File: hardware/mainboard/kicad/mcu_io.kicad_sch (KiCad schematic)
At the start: 30 parts, among them J2 Hirose DM3AT-SF-PEJM5, SW2 BOOT / RECOVERY, SW3 BTN_L1, SW4 BTN_L2, SW5 BTN_R1, SW6 BTN_R2, U1 ESP32-S3-WROOM-1-N16R8, U5 BMI270, U9 TMUX1101DBVR

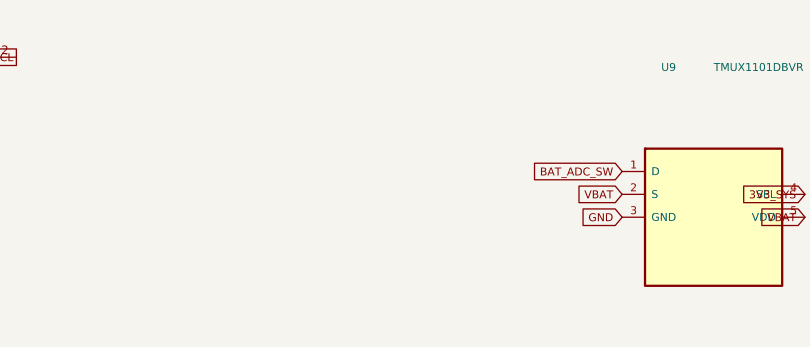
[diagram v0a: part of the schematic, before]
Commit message: R34: physically justified ERC power source flags on switched SYS_EN and pack GND
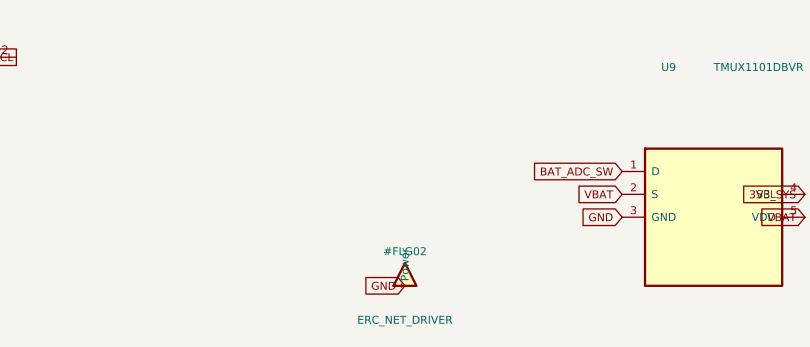
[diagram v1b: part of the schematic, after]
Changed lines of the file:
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@@
 	(global_label "3V3_SYS" (shape input) (at 359.41 182.88 0) (effects (font (size 0.88 0.88)) (justify right bottom)))
 	(global_label "GND" (shape input) (at 374.65 182.88 180) (effects (font (size 0.88 0.88)) (justify right bottom)))
+	(symbol (lib_id "ENKU:ERC_NET_DRIVER") (at 295.91 182.88 0) (unit 1) (exclude_from_sim no) (in_bom no) (on_board no) (dnp no)
+  (property "Reference" "#FLG02" (at 295.91 179.07 0) (effects (font (size 0.88 0.88))))
+  (property "Value" "ERC_NET_DRIVER" (at 295.91 186.69 0) (effects (font (size 0.88 0.88))))
+  (property "Footprint" "" (at 295.91 182.88 0) (effects (font (size 0.88 0.88)) (hide yes)))
+  (property "Datasheet" "~" (at 295.91 182.88 0) (effects (font (size 0.88 0.88)) (hide yes)))
+  (pin "1")
+  (instances (project "enku-mainboard-r0.1" (path "/10000000-0000-4000-8000-000000000001/e4200000-0000-4000-8000-000000000020" (reference "#FLG02") (unit 1))))
 )
+(global_label "GND" (shape input) (at 295.91 182.88 0) (effects (font (size 0.88 0.88)) (justify right bottom)))
+)

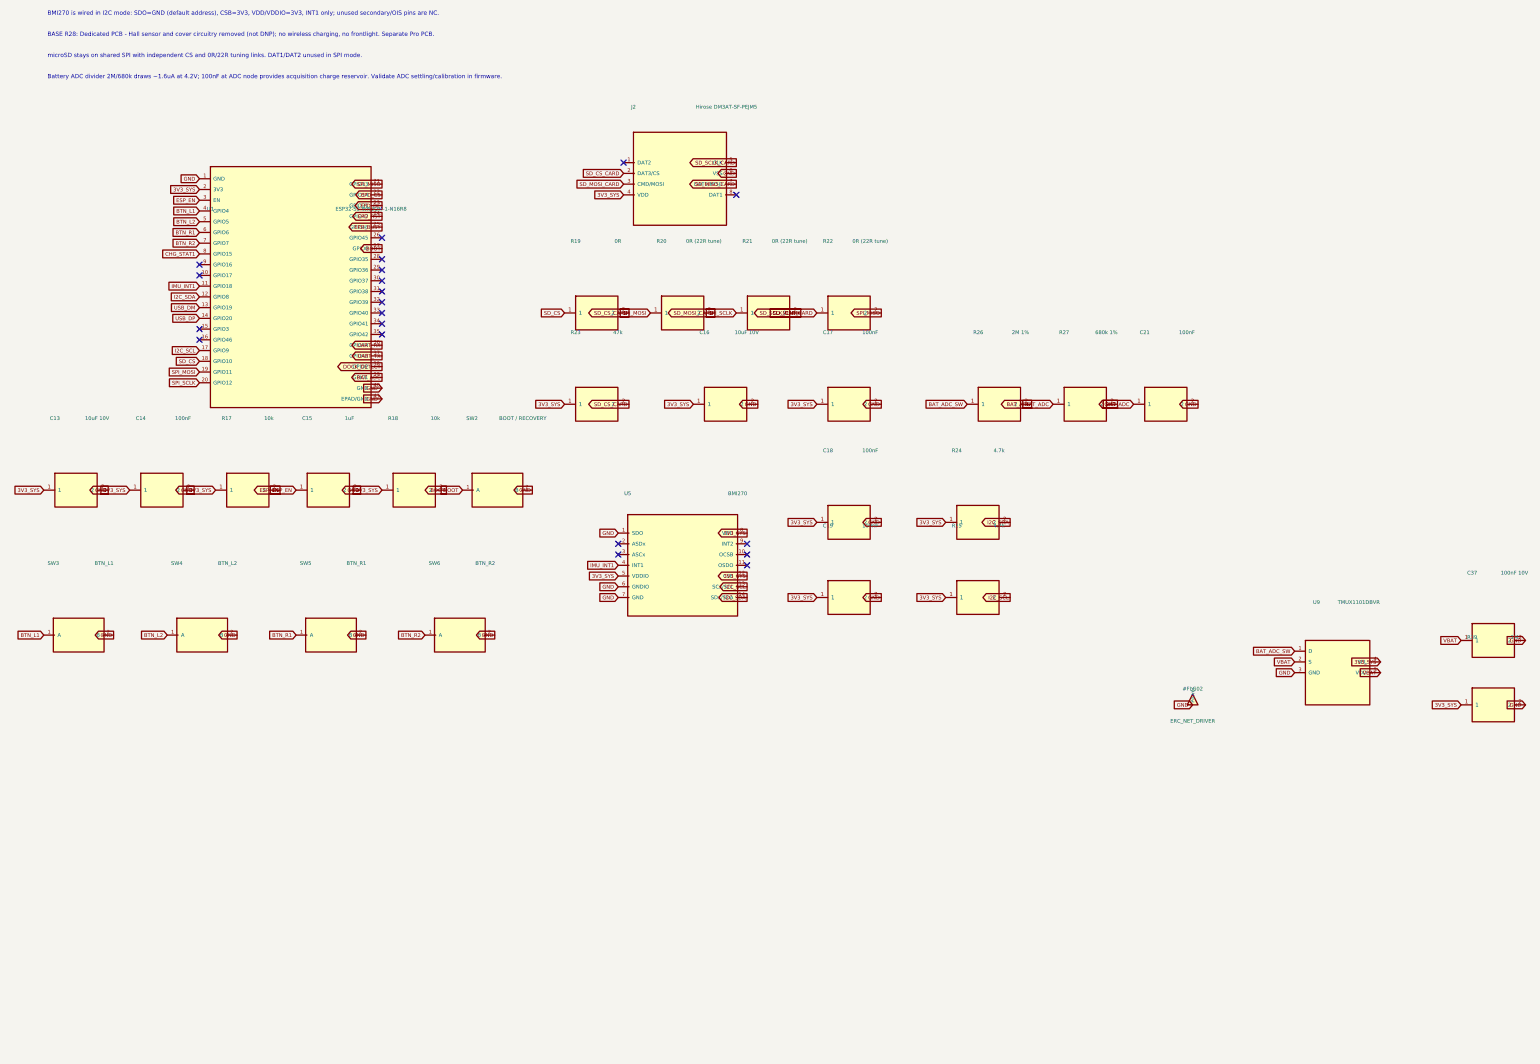
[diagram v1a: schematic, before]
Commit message: R41: implement switched-rail fail-safe VBUS comparator, discharge model, SD supply and dual ground references
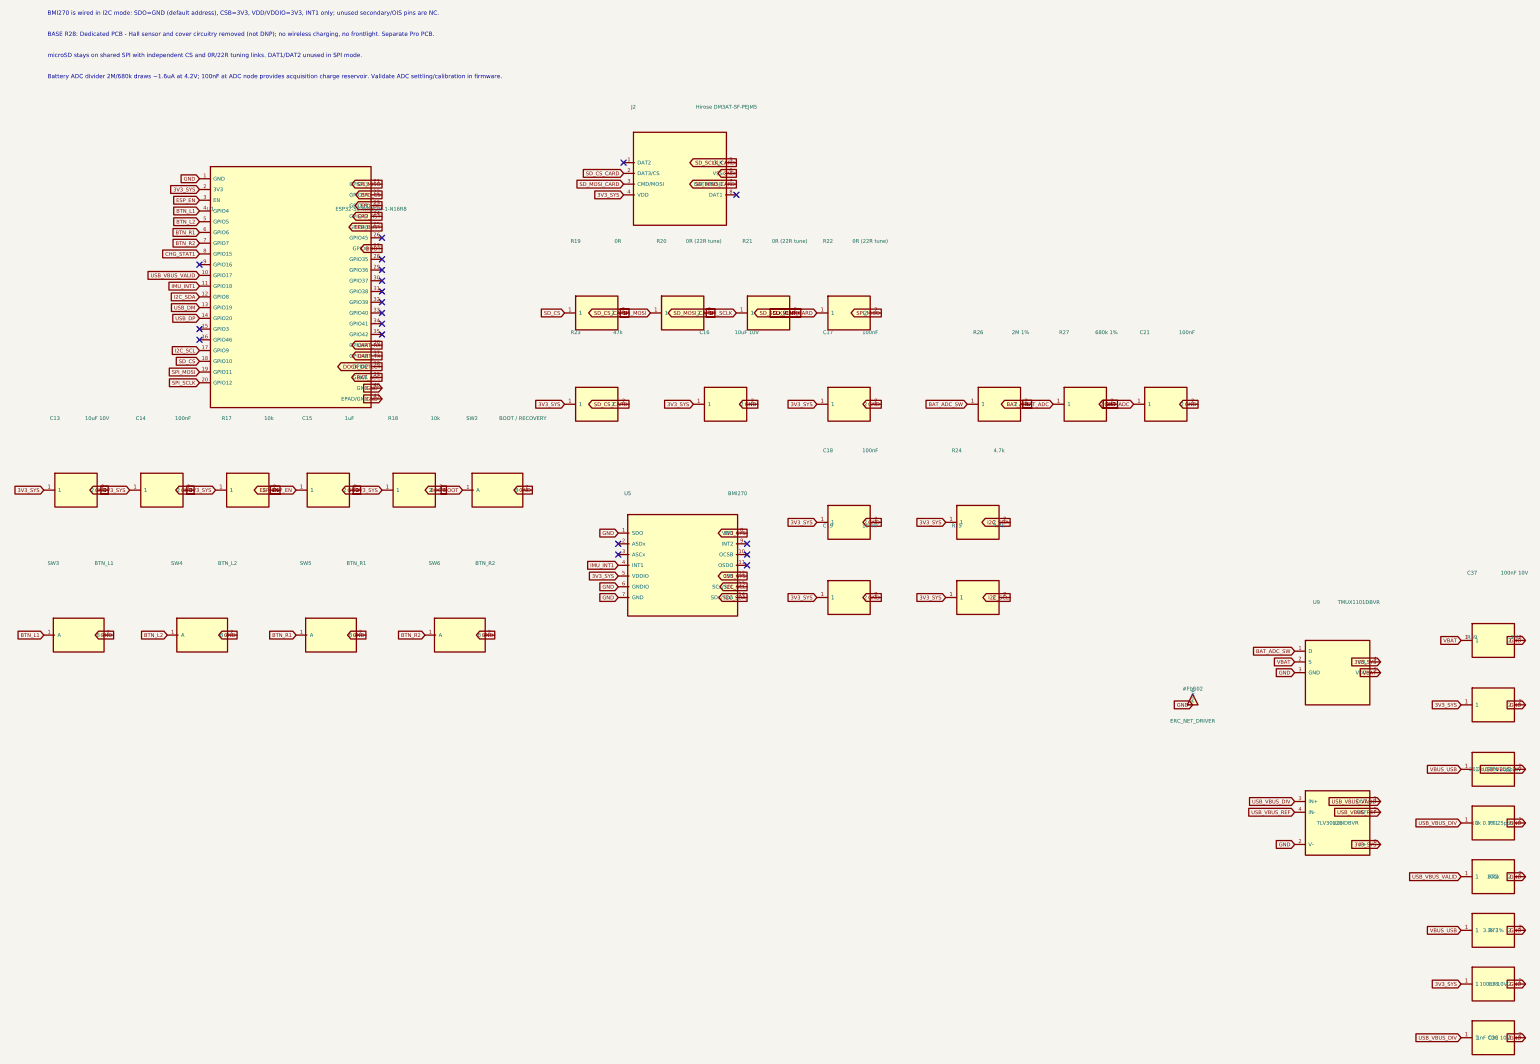
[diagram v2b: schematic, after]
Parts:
- added C38: 100nF 10V, Capacitor_SMD:C_0603_1608Metric, symbol ENKU:C
- added C39: 1nF C0G 10V, Capacitor_SMD:C_0603_1608Metric, symbol ENKU:C
- added R70: 26.7k 0.1% 25ppm, Resistor_SMD:R_0603_1608Metric, symbol ENKU:R
- added R71: 10k 0.1% 25ppm, Resistor_SMD:R_0603_1608Metric, symbol ENKU:R
- added R72: 100k, Resistor_SMD:R_0603_1608Metric, symbol ENKU:R
- added R73: 3.3k 1%, Resistor_SMD:R_0603_1608Metric, symbol ENKU:R
- added U10: TLV3012BIDBVR, ENKU:TLV3012B_DBV0006A, symbol ENKU:TLV3012B
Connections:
- net 3V3_SYS: now also C38.1, U10.6 (V+)
- net GND: now also C38.2, C39.2, R71.2, R72.2, R73.2, U10.2 (V-)
- net USB_VBUS_VALID: now reaches U1.10 (GPIO17)
- net USB_VBUS_VALID: now also R72.1, U10.1 (OUT)
- new net USB_VBUS_DIV: C39.1, R70.2, R71.1, U10.3 (IN+)
- new net USB_VBUS_REF: U10.4 (IN-), U10.5 (REF)
- new net VBUS_USB: R70.1, R73.1
- no-connect marks 20 -> 19
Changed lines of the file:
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@@
 	(global_label "CHG_STAT1" (shape input) (at 60.96 76.2 0) (effects (font (size 0.88 0.88)) (justify right bottom)))
 	(no_connect (at 60.96 78.74))
-	(no_connect (at 60.96 81.28))
+	(global_label "USB_VBUS_VALID" (shape input) (at 60.96 81.28 0) (effects (font (size 0.88 0.88)) (justify right bottom)))
 	(global_label "IMU_INT1" (shape input) (at 60.96 83.82 0) (effects (font (size 0.88 0.88)) (justify right bottom)))
 	(global_label "I2C_SDA" (shape input) (at 60.96 86.36 0) (effects (font (size 0.88 0.88)) (justify right bottom)))
@@
 )
 (global_label "GND" (shape input) (at 295.91 182.88 0) (effects (font (size 0.88 0.88)) (justify right bottom)))
+(symbol (lib_id "ENKU:TLV3012B") (at 330.2 210.82 0) (unit 1) (exclude_from_sim no) (in_bom yes) (on_board yes) (dnp no)
+(property "Reference" "U10" (at 330.2 210.82 0) (effects (font (size 0.88 0.88))))
+(property "Value" "TLV3012BIDBVR" (at 330.2 210.82 0) (effects (font (size 0.88 0.88))))
+(property "Footprint" "ENKU:TLV3012B_DBV0006A" (at 330.2 210.82 0) (effects (font (size 0.88 0.88)) (hide yes)))
+(property "Datasheet" "https://www.ti.com/lit/gpn/TLV3012B" (at 330.2 210.82 0) (effects (font (size 0.88 0.88)) (hide yes)))
+(property "Description" "TLV3012BIDBVR" (at 330.2 210.82 0) (effects (font (size 0.88 0.88)) (hide yes)))
+(pin "1")
+(pin "2")
+(pin "3")
+(pin "4")
+(pin "5")
+(pin "6")
+(instances (project "enku-mainboard-r0.1" (path "/10000000-0000-4000-8000-000000000001/769db365-4ac6-4285-9803-94ba4cec03fc" (reference "U10") (unit 1)))))
+(global_label "USB_VBUS_VALID" (shape input) (at 340.36 205.74 180) (effects (font (size 0.88 0.88)) (justify right bottom)))
+(global_label "GND" (shape input) (at 320.04 215.9 0) (effects (font (size 0.88 0.88)) (justify right bottom)))
+(global_label "USB_VBUS_DIV" (shape input) (at 320.04 205.74 0) (effects (font (size 0.88 0.88)) (justify right bottom)))
+(global_label "USB_VBUS_REF" (shape input) (at 320.04 208.28 0) (effects (font (size 0.88 0.88)) (justify right bottom)))
+(global_label "USB_VBUS_REF" (shape input) (at 340.36 208.28 180) (effects (font (size 0.88 0.88)) (justify right bottom)))
+(global_label "3V3_SYS" (shape input) (at 340.36 215.9 180) (effects (font (size 0.88 0.88)) (justify right bottom)))
+(symbol (lib_id "ENKU:R") (at 367.03 198.12 0) (unit 1) (exclude_from_sim no) (in_bom yes) (on_board yes) (dnp no)
+(property "Reference" "R70" (at 367.03 198.12 0) (effects (font (size 0.88 0.88))))
+(property "Value" "26.7k 0.1% 25ppm" (at 367.03 198.12 0) (effects (font (size 0.88 0.88))))
+(property "Footprint" "Resistor_SMD:R_0603_1608Metric" (at 367.03 198.12 0) (effects (font (size 0.88 0.88)) (hide yes)))
+(property "Datasheet" "~" (at 367.03 198.12 0) (effects (font (size 0.88 0.88)) (hide yes)))
+(property "Description" "26.7k 0.1% 25ppm" (at 367.03 198.12 0) (effects (font (size 0.88 0.88)) (hide yes)))
+(pin "1")
+(pin "2")
+(instances (project "enku-mainboard-r0.1" (path "/10000000-0000-4000-8000-000000000001/2cecd38a-2345-417f-a782-4582a308ce8d" (reference "R70") (unit 1)))))
+(global_label "VBUS_USB" (shape input) (at 359.41 198.12 0) (effects (font (size 0.88 0.88)) (justify right bottom)))
+(global_label "USB_VBUS_DIV" (shape input) (at 374.65 198.12 180) (effects (font (size 0.88 0.88)) (justify right bottom)))
+(symbol (lib_id "ENKU:R") (at 367.03 210.82 0) (unit 1) (exclude_from_sim no) (in_bom yes) (on_board yes) (dnp no)
+(property "Reference" "R71" (at 367.03 210.82 0) (effects (font (size 0.88 0.88))))
+(property "Value" "10k 0.1% 25ppm" (at 367.03 210.82 0) (effects (font (size 0.88 0.88))))
+(property "Footprint" "Resistor_SMD:R_0603_1608Metric" (at 367.03 210.82 0) (effects (font (size 0.88 0.88)) (hide yes)))
+(property "Datasheet" "~" (at 367.03 210.82 0) (effects (font (size 0.88 0.88)) (hide yes)))
+(property "Description" "10k 0.1% 25ppm" (at 367.03 210.82 0) (effects (font (size 0.88 0.88)) (hide yes)))
+(pin "1")
+(pin "2")
+(instances (project "enku-mainboard-r0.1" (path "/10000000-0000-4000-8000-000000000001/c6ce4a4a-ea41-42a2-b971-307e49b77f8a" (reference "R71") (unit 1)))))
+(global_label "USB_VBUS_DIV" (shape input) (at 359.41 210.82 0) (effects (font (size 0.88 0.88)) (justify right bottom)))
+(global_label "GND" (shape input) (at 374.65 210.82 180) (effects (font (size 0.88 0.88)) (justify right bottom)))
+(symbol (lib_id "ENKU:R") (at 367.03 223.52 0) (unit 1) (exclude_from_sim no) (in_bom yes) (on_board yes) (dnp no)
+(property "Reference" "R72" (at 367.03 223.52 0) (effects (font (size 0.88 0.88))))
+(property "Value" "100k" (at 367.03 223.52 0) (effects (font (size 0.88 0.88))))
+(property "Footprint" "Resistor_SMD:R_0603_1608Metric" (at 367.03 223.52 0) (effects (font (size 0.88 0.88)) (hide yes)))
+(property "Datasheet" "~" (at 367.03 223.52 0) (effects (font (size 0.88 0.88)) (hide yes)))
+(property "Description" "100k" (at 367.03 223.52 0) (effects (font (size 0.88 0.88)) (hide yes)))
+(pin "1")
+(pin "2")
+(instances (project "enku-mainboard-r0.1" (path "/10000000-0000-4000-8000-000000000001/13fd1e8d-530d-494a-999d-def73aecf99f" (reference "R72") (unit 1)))))
+(global_label "USB_VBUS_VALID" (shape input) (at 359.41 223.52 0) (effects (font (size 0.88 0.88)) (justify right bottom)))
+(global_label "GND" (shape input) (at 374.65 223.52 180) (effects (font (size 0.88 0.88)) (justify right bottom)))
+(symbol (lib_id "ENKU:R") (at 367.03 236.22 0) (unit 1) (exclude_from_sim no) (in_bom yes) (on_board yes) (dnp no)
+(property "Reference" "R73" (at 367.03 236.22 0) (effects (font (size 0.88 0.88))))
+(property "Value" "3.3k 1%" (at 367.03 236.22 0) (effects (font (size 0.88 0.88))))
+(property "Footprint" "Resistor_SMD:R_0603_1608Metric" (at 367.03 236.22 0) (effects (font (size 0.88 0.88)) (hide yes)))
+(property "Datasheet" "~" (at 367.03 236.22 0) (effects (font (size 0.88 0.88)) (hide yes)))
+(property "Description" "3.3k 1%" (at 367.03 236.22 0) (effects (font (size 0.88 0.88)) (hide yes)))
+(pin "1")
+(pin "2")
+(instances (project "enku-mainboard-r0.1" (path "/10000000-0000-4000-8000-000000000001/aea14dbc-4838-4aec-baec-98e56acbf733" (reference "R73") (unit 1)))))
+(global_label "VBUS_USB" (shape input) (at 359.41 236.22 0) (effects (font (size 0.88 0.88)) (justify right bottom)))
+(global_label "GND" (shape input) (at 374.65 236.22 180) (effects (font (size 0.88 0.88)) (justify right bottom)))
+(symbol (lib_id "ENKU:C") (at 367.03 248.92000000000002 0) (unit 1) (exclude_from_sim no) (in_bom yes) (on_board yes) (dnp no)
+(property "Reference" "C38" (at 367.03 248.92000000000002 0) (effects (font (size 0.88 0.88))))
+(property "Value" "100nF 10V" (at 367.03 248.92000000000002 0) (effects (font (size 0.88 0.88))))
+(property "Footprint" "Capacitor_SMD:C_0603_1608Metric" (at 367.03 248.92000000000002 0) (effects (font (size 0.88 0.88)) (hide yes)))
+(property "Datasheet" "~" (at 367.03 248.92000000000002 0) (effects (font (size 0.88 0.88)) (hide yes)))
+(property "Description" "100nF 10V" (at 367.03 248.92000000000002 0) (effects (font (size 0.88 0.88)) (hide yes)))
+(pin "1")
+(pin "2")
+(instances (project "enku-mainboard-r0.1" (path "/10000000-0000-4000-8000-000000000001/f0ad38fb-f5c1-4281-a0c9-eb89c1e529c3" (reference "C38") (unit 1)))))
+(global_label "3V3_SYS" (shape input) (at 359.41 248.92 0) (effects (font (size 0.88 0.88)) (justify right bottom)))
+(global_label "GND" (shape input) (at 374.65 248.92 180) (effects (font (size 0.88 0.88)) (justify right bottom)))
+(symbol (lib_id "ENKU:C") (at 367.03 261.62 0) (unit 1) (exclude_from_sim no) (in_bom yes) (on_board yes) (dnp no)
+(property "Reference" "C39" (at 367.03 261.62 0) (effects (font (size 0.88 0.88))))
+(property "Value" "1nF C0G 10V" (at 367.03 261.62 0) (effects (font (size 0.88 0.88))))
+(property "Footprint" "Capacitor_SMD:C_0603_1608Metric" (at 367.03 261.62 0) (effects (font (size 0.88 0.88)) (hide yes)))
+(property "Datasheet" "~" (at 367.03 261.62 0) (effects (font (size 0.88 0.88)) (hide yes)))
+(property "Description" "1nF C0G 10V" (at 367.03 261.62 0) (effects (font (size 0.88 0.88)) (hide yes)))
+(pin "1")
+(pin "2")
+(instances (project "enku-mainboard-r0.1" (path "/10000000-0000-4000-8000-000000000001/88d89a42-f9c1-4813-b5a8-4c31ebfec0a8" (reference "C39") (unit 1)))))
+(global_label "USB_VBUS_DIV" (shape input) (at 359.41 261.62 0) (effects (font (size 0.88 0.88)) (justify right bottom)))
+(global_label "GND" (shape input) (at 374.65 261.62 180) (effects (font (size 0.88 0.88)) (justify right bottom)))
 )
